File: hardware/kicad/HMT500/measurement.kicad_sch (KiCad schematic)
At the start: 15 parts, among them J3 SM04B-SRSS-TB, U5 PCAP04-AQFM-24, U6 ADS1220IPWR

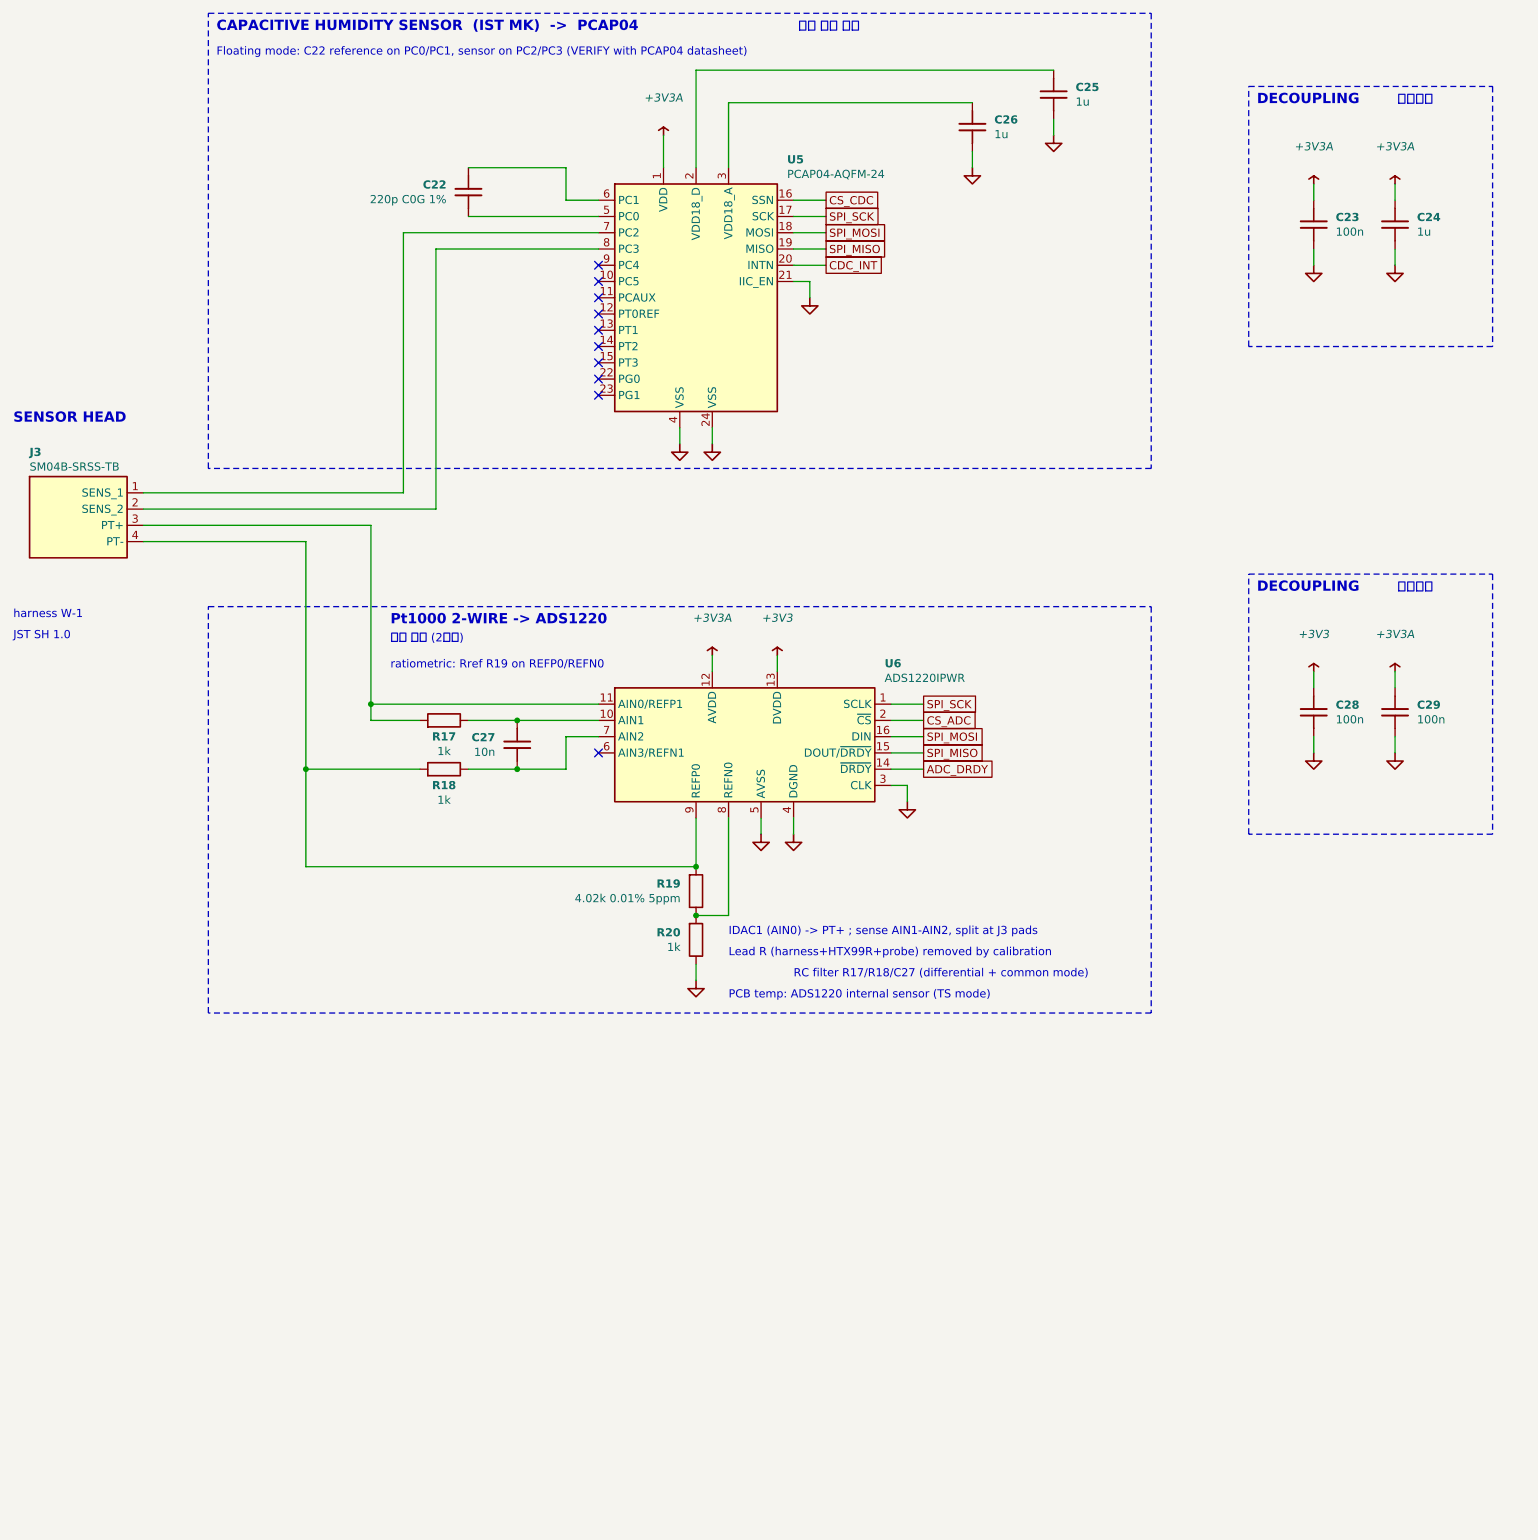
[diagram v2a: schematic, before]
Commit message: Schematic redraw: aligned parts, straight wires, fewer junctions
- Bends 54 -> 1, junctions 51 -> 31 (remaining are real 3-way nodes: divider taps,
  protection taps, tied pin pairs, power flags)
- Power pins get their own power symbols instead of rails with T-branches; signals
  between distant parts use labels; two-pin parts sit on the pin row they connect to
- Symbol pin order rearranged for straight runs (pin numbers unchanged): TPS2660,
  LMR36006 (BOOT on top), PCAP04 (Cref pins 3 rows apart, VDD18 on right), ADS1220
  (bottom pins 3 apart), DAC8760 (GND-tied pins on bottom), TPS26611 (FLT on bottom)
- New checks: pin names inside IC bodies must not overlap, boxes must not overlap;
  test limits bends per sheet and total junctions
- Netlist check 63 nets, 0 errors

Co-Authored-By: Claude Opus 5.5 <noreply@anthropic.com>
Claude-Session: https://claude.ai/code/session_01JA2o8uJsqp9Vzsg4b665ev
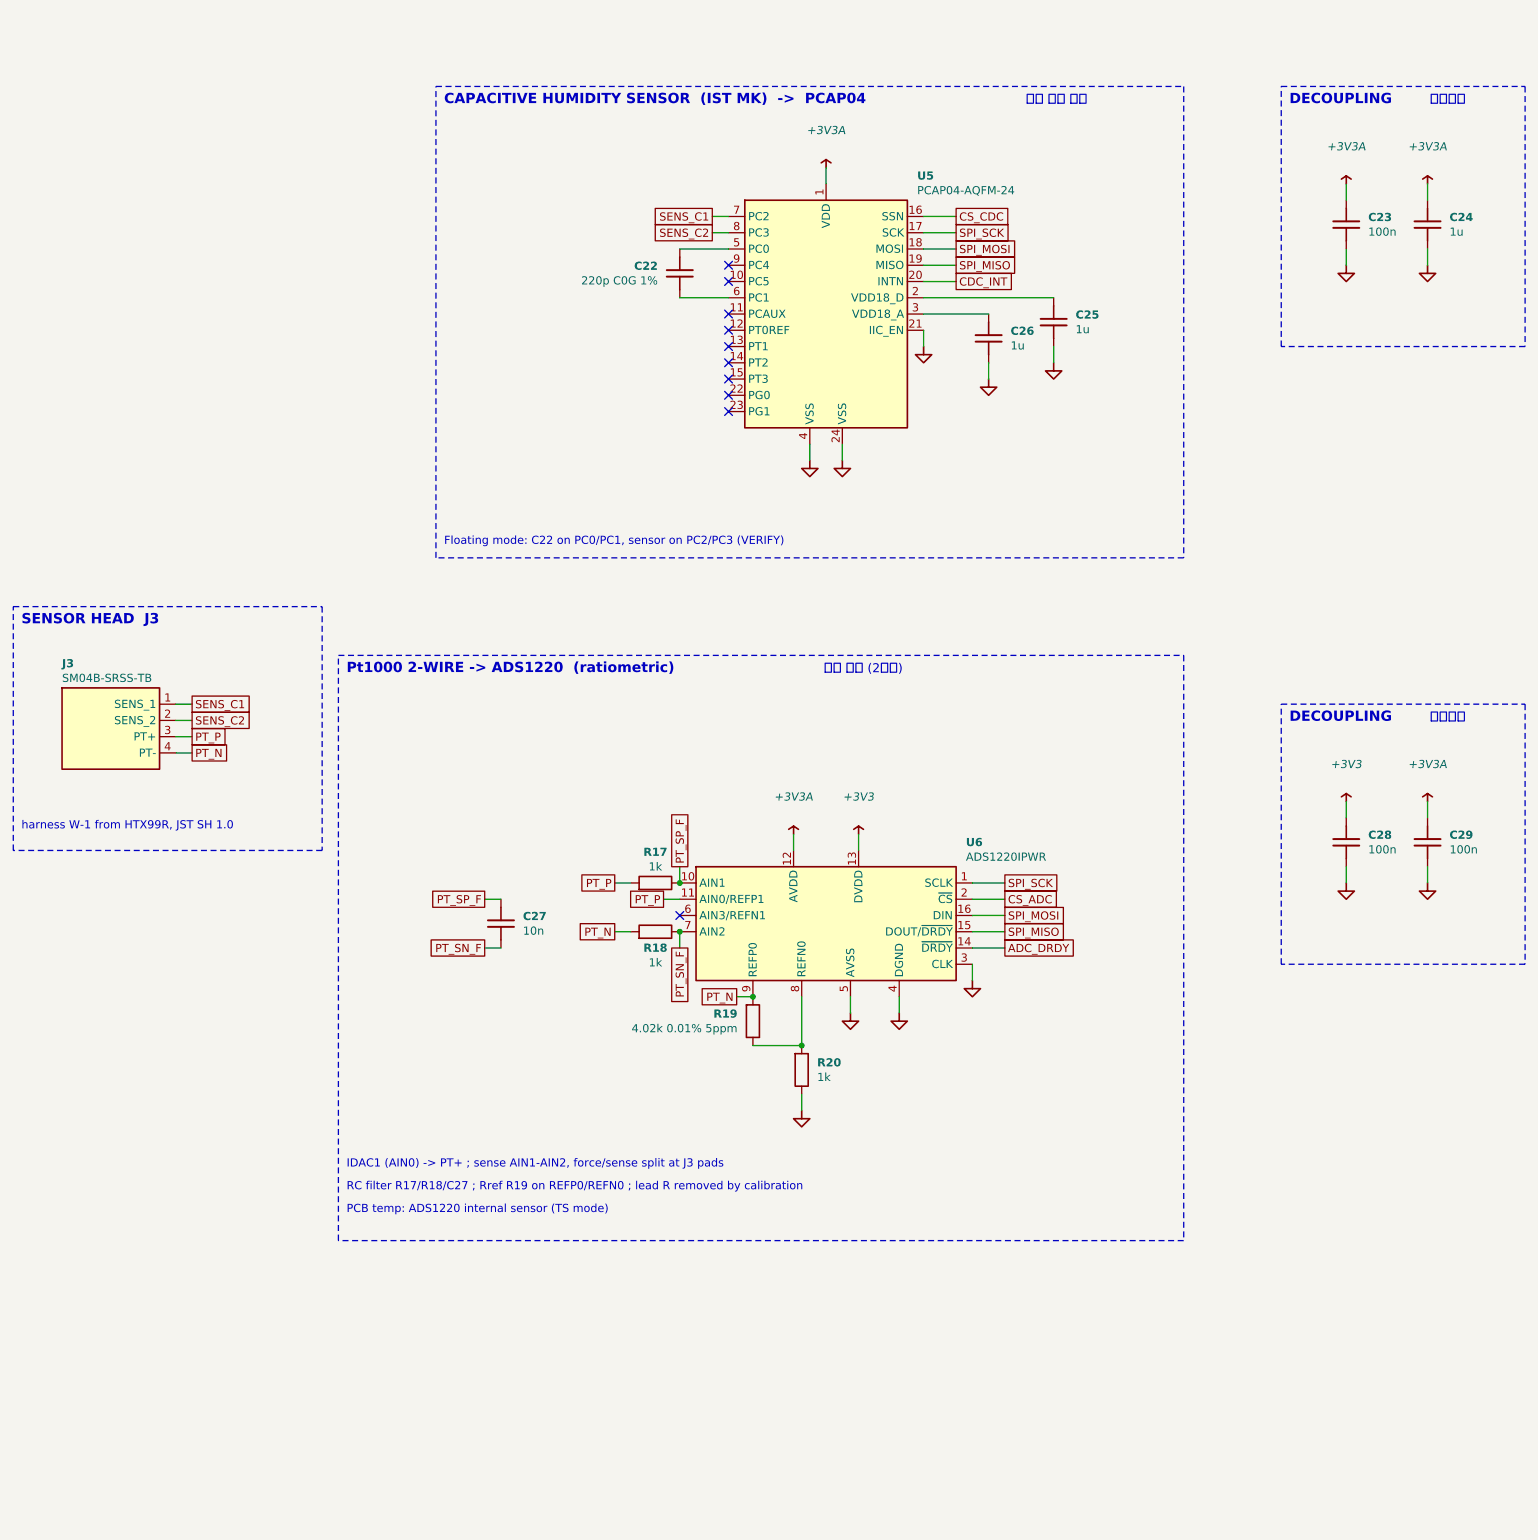
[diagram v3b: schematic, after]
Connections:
- net PT_SP_F: now reaches C27.1, R17.2, U6.10 (AIN1)
- net PT_P: now reaches J3.3 (PT+), R17.1, U6.11 (AIN0/REFP1)
- net PT_SN_F: now reaches C27.2, R18.2, U6.7 (AIN2)
- net PT_N: now reaches J3.4 (PT-), R18.1, R19.1, U6.9 (REFP0)
- net at C22.1: now also U5.5 (PC0); no longer U5.6 (PC1)
- net at C22.2: now also U5.6 (PC1); no longer U5.5 (PC0)
- net SENS_C1: now reaches J3.1 (SENS_1), U5.7 (PC2)
- net SENS_C2: now reaches J3.2 (SENS_2), U5.8 (PC3)
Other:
- note added: "Floating mode: C22 on PC0/PC1, sensor on PC2/PC3 (VERIFY)"
- note added: "IDAC1 (AIN0) -> PT+ ; sense AIN1-AIN2, force/sense split at J3 pads"
- note added: "Pt1000 2-WIRE -> ADS1220 (ratiometric)"
- note added: "RC filter R17/R18/C27 ; Rref R19 on REFP0/REFN0 ; lead R removed by calibration"
- note added: "SENSOR HEAD J3"
- note added: "harness W-1 from HTX99R, JST SH 1.0"
- note removed: "Floating mode: C22 reference on PC0/PC1, sensor on PC2/PC3 (VERIFY with PCAP04 datasheet)"
- note removed: "IDAC1 (AIN0) -> PT+ ; sense AIN1-AIN2, split at J3 pads"
- note removed: "JST SH 1.0"
- note removed: "Lead R (harness+HTX99R+probe) removed by calibration"
- note removed: "Pt1000 2-WIRE -> ADS1220"
- note removed: "RC filter R17/R18/C27 (differential + common mode)"
- note removed: "SENSOR HEAD"
- note removed: "harness W-1"
- note removed: "ratiometric: Rref R19 on REFP0/REFN0"
- moved on the sheet: C22, C23, C24, C25, C26, C27, C28, C29, J3, R17, R18, R19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

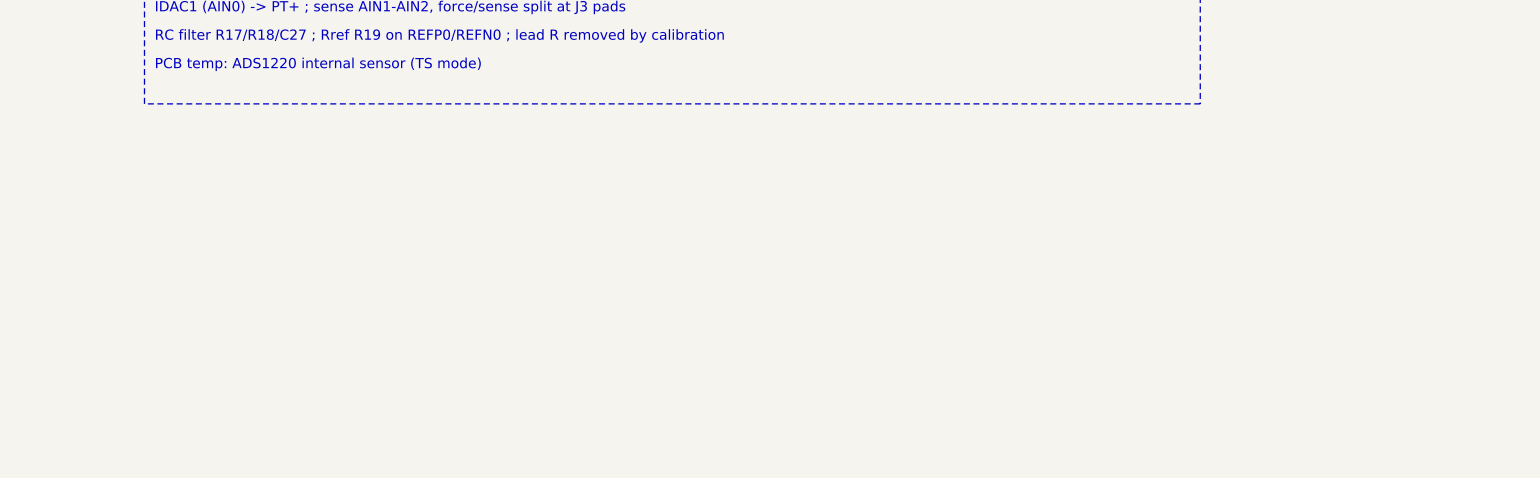
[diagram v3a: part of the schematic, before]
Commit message: Schematic: key-parts table (role, features, specs) on every sheet
- Aligned 4-column table per sheet: reference, part, role, features/specs;
  values still to confirm against datasheets marked with *
- Connector and RS-485 sheets moved to A3 for room
- New checks: text and boxes stay inside the page and out of the title block;
  every character of Hangul text must exist in NanumGothic (minus sign and micro
  sign substituted)

Co-Authored-By: Claude Opus 5.5 <noreply@anthropic.com>
Claude-Session: https://claude.ai/code/session_01JA2o8uJsqp9Vzsg4b665ev
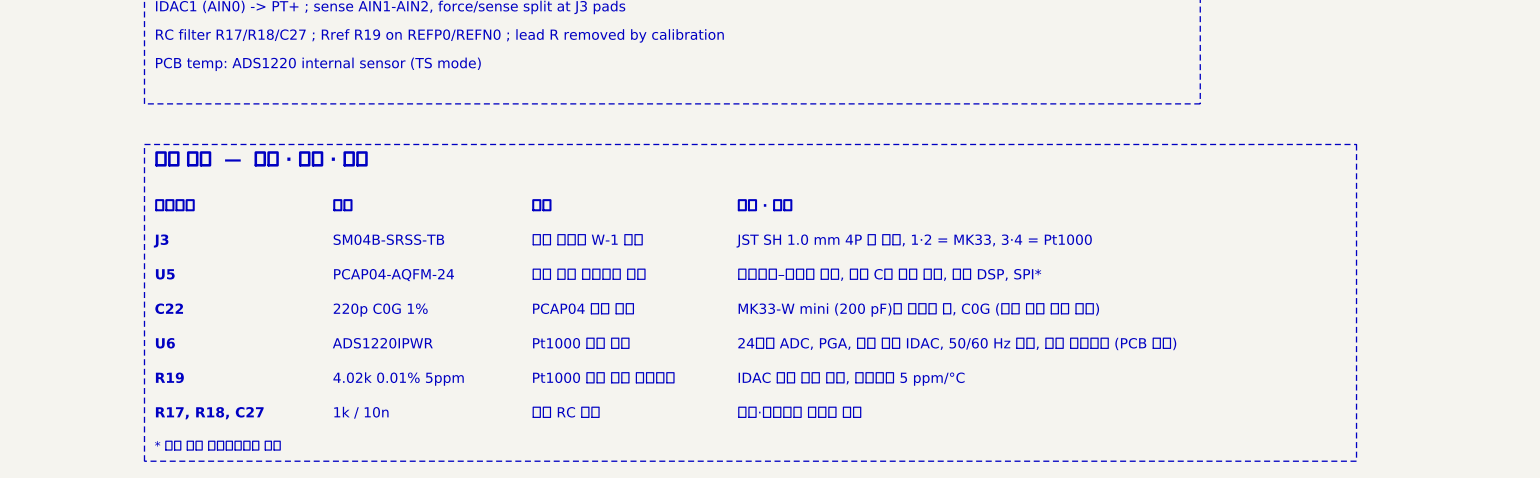
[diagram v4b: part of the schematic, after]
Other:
- note added: "* 표시 값은 데이터시트로 확인"
- note added: "1k / 10n"
- note added: "220p C0G 1%"
- note added: "24비트 ADC, PGA, 여기 전류 IDAC, 50/60 Hz 제거, 내부 온도센서 (PCB 온도)"
- note added: "4.02k 0.01% 5ppm"
- note added: "ADS1220IPWR"
- note added: "C22"
- note added: "IDAC 전류 오차 상쇄, 온도계수 5 ppm/°C"
- note added: "J3"
- note added: "JST SH 1.0 mm 4P 옆 삽입, 1·2 = MK33, 3·4 = Pt1000"
- note added: "MK33-W mini (200 pF)와 비슷한 값, C0G (온도 변화 거의 없음)"
- note added: "PCAP04 기준 용량"
- note added: "PCAP04-AQFM-24"
- note added: "Pt1000 비율 측정 기준저항"
- note added: "Pt1000 온도 측정"
- note added: "R17, R18, C27"
- note added: "R19"
- note added: "SM04B-SRSS-TB"
- note added: "U5"
- note added: "U6"
- note added: "부품"
- note added: "부품번호"
- note added: "센서 하네스 W-1 연결"
- note added: "습도 센서 정전용량 측정"
- note added: "역할"
- note added: "입력 RC 필터"
- note added: "정전용량–디지털 변환, 기준 C와 비율 측정, 내부 DSP, SPI*"
- note added: "주요 부품 — 역할 · 특징 · 사양"
- note added: "차동·공통모드 노이즈 제거"
- note added: "특징 · 사양"
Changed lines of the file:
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@@
 (rectangle (start 213.36 38.1) (end 251.46 78.74) (stroke (width 0.1524) (type dash) (color 72 72 160 1)) (fill (type none)))
 (rectangle (start 213.36 134.62) (end 251.46 175.26) (stroke (width 0.1524) (type dash) (color 72 72 160 1)) (fill (type none)))
+(rectangle (start 66.04 223.52) (end 217.668 263.144) (stroke (width 0.1524) (type dash) (color 72 72 160 1)) (fill (type none)))
 (text "SENSOR HEAD  J3" (at 16.51 122.428 0) (effects (font (size 1.6 1.6) bold) (justify left bottom)))
 (text "harness W-1 from HTX99R, JST SH 1.0" (at 16.51 154.432 0) (effects (font (size 1.27 1.27)) (justify left bottom)))
@@
 (text "DECOUPLING" (at 214.63 137.668 0) (effects (font (size 1.6 1.6) bold) (justify left bottom)))
 (text "바이패스" (at 236.584 137.668 0) (effects (font (face "NanumGothic") (size 1.4 1.4)) (justify left bottom)))
+(text "부품번호" (at 67.31 232.156 0) (effects (font (face "NanumGothic") (size 1.27 1.27) bold) (justify left bottom)))
+(text "부품" (at 89.5883 232.156 0) (effects (font (face "NanumGothic") (size 1.27 1.27) bold) (justify left bottom)))
+(text "역할" (at 114.48 232.156 0) (effects (font (face "NanumGothic") (size 1.27 1.27) bold) (justify left bottom)))
+(text "특징 · 사양" (at 140.198 232.156 0) (effects (font (face "NanumGothic") (size 1.27 1.27) bold) (justify left bottom)))
+(text "J3" (at 67.31 236.474 0) (effects (font (size 1.27 1.27) bold) (justify left bottom)))
+(text "SM04B-SRSS-TB" (at 89.5883 236.474 0) (effects (font (size 1.27 1.27)) (justify left bottom)))
+(text "센서 하네스 W-1 연결" (at 114.48 236.474 0) (effects (font (face "NanumGothic") (size 1.27 1.27)) (justify left bottom)))
+(text "JST SH 1.0 mm 4P 옆 삽입, 1·2 = MK33, 3·4 = Pt1000" (at 140.198 236.474 0) (effects (font (face "NanumGothic") (size 1.27 1.27)) (justify left bottom)))
+(text "U5" (at 67.31 240.792 0) (effects (font (size 1.27 1.27) bold) (justify left bottom)))
+(text "PCAP04-AQFM-24" (at 89.5883 240.792 0) (effects (font (size 1.27 1.27)) (justify left bottom)))
+(text "습도 센서 정전용량 측정" (at 114.48 240.792 0) (effects (font (face "NanumGothic") (size 1.27 1.27)) (justify left bottom)))
+(text "정전용량–디지털 변환, 기준 C와 비율 측정, 내부 DSP, SPI*" (at 140.198 240.792 0) (effects (font (face "NanumGothic") (size 1.27 1.27)) (justify left bottom)))
+(text "C22" (at 67.31 245.11 0) (effects (font (size 1.27 1.27) bold) (justify left bottom)))
+(text "220p C0G 1%" (at 89.5883 245.11 0) (effects (font (size 1.27 1.27)) (justify left bottom)))
+(text "PCAP04 기준 용량" (at 114.48 245.11 0) (effects (font (face "NanumGothic") (size 1.27 1.27)) (justify left bottom)))
+(text "MK33-W mini (200 pF)와 비슷한 값, C0G (온도 변화 거의 없음)" (at 140.198 245.11 0) (effects (font (face "NanumGothic") (size 1.27 1.27)) (justify left bottom)))
+(text "U6" (at 67.31 249.428 0) (effects (font (size 1.27 1.27) bold) (justify left bottom)))
+(text "ADS1220IPWR" (at 89.5883 249.428 0) (effects (font (size 1.27 1.27)) (justify left bottom)))
+(text "Pt1000 온도 측정" (at 114.48 249.428 0) (effects (font (face "NanumGothic") (size 1.27 1.27)) (justify left bottom)))
+(text "24비트 ADC, PGA, 여기 전류 IDAC, 50/60 Hz 제거, 내부 온도센서 (PCB 온도)" (at 140.198 249.428 0) (effects (font (face "NanumGothic") (size 1.27 1.27)) (justify left bottom)))
+(text "R19" (at 67.31 253.746 0) (effects (font (size 1.27 1.27) bold) (justify left bottom)))
+(text "4.02k 0.01% 5ppm" (at 89.5883 253.746 0) (effects (font (size 1.27 1.27)) (justify left bottom)))
+(text "Pt1000 비율 측정 기준저항" (at 114.48 253.746 0) (effects (font (face "NanumGothic") (size 1.27 1.27)) (justify left bottom)))
+(text "IDAC 전류 오차 상쇄, 온도계수 5 ppm/°C" (at 140.198 253.746 0) (effects (font (face "NanumGothic") (size 1.27 1.27)) (justify left bottom)))
+(text "R17, R18, C27" (at 67.31 258.064 0) (effects (font (size 1.27 1.27) bold) (justify left bottom)))
+(text "1k / 10n" (at 89.5883 258.064 0) (effects (font (size 1.27 1.27)) (justify left bottom)))
+(text "입력 RC 필터" (at 114.48 258.064 0) (effects (font (face "NanumGothic") (size 1.27 1.27)) (justify left bottom)))
+(text "차동·공통모드 노이즈 제거" (at 140.198 258.064 0) (effects (font (face "NanumGothic") (size 1.27 1.27)) (justify left bottom)))
+(text "주요 부품  —  역할 · 특징 · 사양" (at 67.31 226.568 0) (effects (font (face "NanumGothic") (size 1.6 1.6) bold) (justify left bottom)))
+(text "* 표시 값은 데이터시트로 확인" (at 67.31 262.128 0) (effects (font (face "NanumGothic") (size 1.1 1.1)) (justify left bottom)))
 )
